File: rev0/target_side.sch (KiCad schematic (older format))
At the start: 8 parts

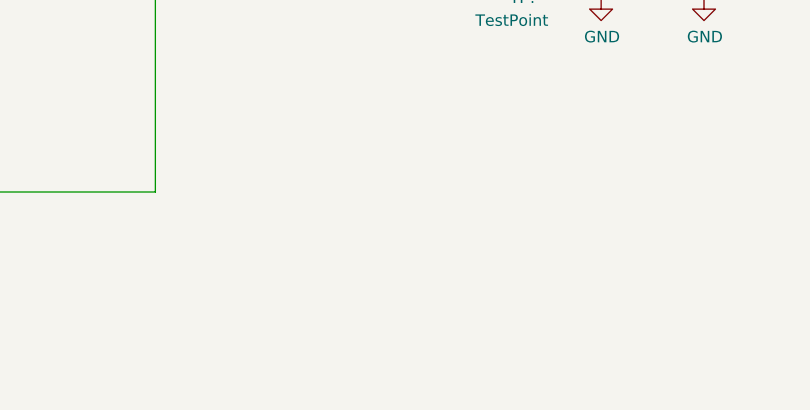
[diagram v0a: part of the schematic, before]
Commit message: schematic: finish initial capture
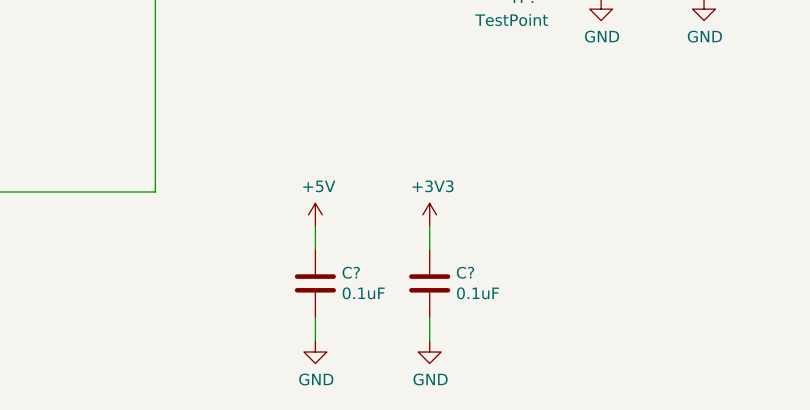
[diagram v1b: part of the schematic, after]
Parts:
- added C? (x2): 0.1uF, symbol Device:C
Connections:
- wire segments 63 -> 67
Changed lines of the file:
@@
 $Descr A4 11693 8268
 encoding utf-8
-Sheet 6 6
-Title ""
-Date ""
-Rev ""
-Comp ""
-Comment1 ""
+Sheet 5 9
+Title "LUNA: Downstream / Target / Analysis Section"
+Date "2019-10-20"
+Rev "r0"
+Comp "Great Scott Gadgets"
+Comment1 "Katherine J. Temkin"
 Comment2 ""
-Comment3 ""
+Comment3 "Licensed under the CERN OHL v1.2"
 Comment4 ""
 $EndDescr
@@
 U 1 1 5DDE2AE4
 P 6500 3750
+AR Path="/5DD754D4/5DDE2AE4" Ref="#PWR?"  Part="1"
+AR Path="/5DDDB747/5DDE2AE4" Ref="#PWR?"  Part="1"
 F 0 "#PWR?" H 6500 3600 50  0001 C CNN
 F 1 "+3V3" V 6515 3878 50  0000 L CNN
@@
 AR Path="/5DCD9772/5DDE2AF8" Ref="R?"  Part="1"
 AR Path="/5DD754D4/5DDE2AF8" Ref="R?"  Part="1"
+AR Path="/5DDDB747/5DDE2AF8" Ref="R?"  Part="1"
 F 0 "R?" V 8250 2800 50  0000 C CNN
 F 1 "20k" V 8300 2950 50  0000 C CNN
@@
 AR Path="/5DCD9772/5DDE2AFF" Ref="#PWR?"  Part="1"
 AR Path="/5DD754D4/5DDE2AFF" Ref="#PWR?"  Part="1"
+AR Path="/5DDDB747/5DDE2AFF" Ref="#PWR?"  Part="1"
 F 0 "#PWR?" H 8600 3250 50  0001 C CNN
 F 1 "GND" V 8605 3372 50  0000 R CNN
@@
 AR Path="/5DCD9772/5DDE2B06" Ref="R?"  Part="1"
 AR Path="/5DD754D4/5DDE2B06" Ref="R?"  Part="1"
+AR Path="/5DDDB747/5DDE2B06" Ref="R?"  Part="1"
 F 0 "R?" V 8200 3350 50  0000 C CNN
 F 1 "8.06k+1%" V 8150 3650 50  0000 C CNN
@@
 AR Path="/5DCD9772/5DDE2B0E" Ref="#PWR?"  Part="1"
 AR Path="/5DD754D4/5DDE2B0E" Ref="#PWR?"  Part="1"
+AR Path="/5DDDB747/5DDE2B0E" Ref="#PWR?"  Part="1"
 F 0 "#PWR?" H 8350 2150 50  0001 C CNN
 F 1 "+3V3" H 8364 2473 50  0000 C CNN
@@
 AR Path="/5DCD9772/5DDE2B14" Ref="#PWR?"  Part="1"
 AR Path="/5DD754D4/5DDE2B14" Ref="#PWR?"  Part="1"
+AR Path="/5DDDB747/5DDE2B14" Ref="#PWR?"  Part="1"
 F 0 "#PWR?" H 8150 2150 50  0001 C CNN
 F 1 "+5V" H 8164 2473 50  0000 C CNN
@@
 AR Path="/5DCD9772/5DDE2B1C" Ref="#PWR?"  Part="1"
 AR Path="/5DD754D4/5DDE2B1C" Ref="#PWR?"  Part="1"
+AR Path="/5DDDB747/5DDE2B1C" Ref="#PWR?"  Part="1"
 F 0 "#PWR?" H 8100 2500 50  0001 C CNN
 F 1 "GND" V 8105 2622 50  0000 R CNN
@@
 AR Path="/5DCD9772/5DDE2B2D" Ref="TP?"  Part="1"
 AR Path="/5DD754D4/5DDE2B2D" Ref="TP?"  Part="1"
+AR Path="/5DDDB747/5DDE2B2D" Ref="TP?"  Part="1"
 F 0 "TP?" H 8050 4600 50  0000 R CNN
 F 1 "TestPoint" H 8200 4700 50  0000 R CNN
@@
 AR Path="/5DCD9772/5DDE2B37" Ref="TP?"  Part="1"
 AR Path="/5DD754D4/5DDE2B37" Ref="TP?"  Part="1"
+AR Path="/5DDDB747/5DDE2B37" Ref="TP?"  Part="1"
 F 0 "TP?" V 9055 4087 50  0000 L CNN
 F 1 "TestPoint" V 9145 4087 50  0000 L CNN
@@
 AR Path="/5DCD9772/5DDE2B42" Ref="#PWR?"  Part="1"
 AR Path="/5DD754D4/5DDE2B42" Ref="#PWR?"  Part="1"
+AR Path="/5DDDB747/5DDE2B42" Ref="#PWR?"  Part="1"
 F 0 "#PWR?" H 8800 4350 50  0001 C CNN
 F 1 "GND" H 8804 4428 50  0000 C CNN
@@
 AR Path="/5DCD9772/5DDE2B48" Ref="C?"  Part="1"
 AR Path="/5DD754D4/5DDE2B48" Ref="C?"  Part="1"
+AR Path="/5DDDB747/5DDE2B48" Ref="C?"  Part="1"
 F 0 "C?" H 8915 4345 50  0000 L CNN
 F 1 "1uF" H 8915 4255 50  0000 L CNN
@@
 AR Path="/5DCD9772/5DDE2B50" Ref="#PWR?"  Part="1"
 AR Path="/5DD754D4/5DDE2B50" Ref="#PWR?"  Part="1"
+AR Path="/5DDDB747/5DDE2B50" Ref="#PWR?"  Part="1"
 F 0 "#PWR?" H 8350 4350 50  0001 C CNN
 F 1 "GND" H 8354 4428 50  0000 C CNN
@@
 AR Path="/5DCD9772/5DDE2B56" Ref="C?"  Part="1"
 AR Path="/5DD754D4/5DDE2B56" Ref="C?"  Part="1"
+AR Path="/5DDDB747/5DDE2B56" Ref="C?"  Part="1"
 F 0 "C?" H 8465 4345 50  0000 L CNN
 F 1 "1uF" H 8465 4255 50  0000 L CNN
@@
 AR Path="/5DCD9772/5DDE2B63" Ref="U?"  Part="1"
 AR Path="/5DD754D4/5DDE2B63" Ref="U?"  Part="1"
+AR Path="/5DDDB747/5DDE2B63" Ref="U?"  Part="1"
 F 0 "U?" H 7250 2613 50  0000 C CNN
 F 1 "USB3343" H 7250 2523 50  0000 C CNN
@@
 	1    0    0    -1
 $EndComp
+$Comp
+L Device:C C?
+U 1 1 5DEDF6B3
+P 7100 5850
+AR Path="/5DCD9772/5DEDF6B3" Ref="C?"  Part="1"
+AR Path="/5DDDB747/5DEDF6B3" Ref="C?"  Part="1"
+F 0 "C?" H 7215 5895 50  0000 L CNN
+F 1 "0.1uF" H 7215 5805 50  0000 L CNN
+F 2 "" H 7138 5700 50  0001 C CNN
+F 3 "~" H 7100 5850 50  0001 C CNN
+	1    7100 5850
+	1    0    0    -1
+$EndComp
+$Comp
+L Device:C C?
+U 1 1 5DEDF6B9
+P 7600 5850
+AR Path="/5DCD9772/5DEDF6B9" Ref="C?"  Part="1"
+AR Path="/5DDDB747/5DEDF6B9" Ref="C?"  Part="1"
+F 0 "C?" H 7715 5895 50  0000 L CNN
+F 1 "0.1uF" H 7715 5805 50  0000 L CNN
+F 2 "" H 7638 5700 50  0001 C CNN
+F 3 "~" H 7600 5850 50  0001 C CNN
+	1    7600 5850
+	1    0    0    -1
+$EndComp
+$Comp
+L power:+5V #PWR?
+U 1 1 5DEDF6BF
+P 7100 5600
+AR Path="/5DCD9772/5DEDF6BF" Ref="#PWR?"  Part="1"
+AR Path="/5DDDB747/5DEDF6BF" Ref="#PWR?"  Part="1"
+F 0 "#PWR?" H 7100 5450 50  0001 C CNN
+F 1 "+5V" H 7114 5773 50  0000 C CNN
+F 2 "" H 7100 5600 50  0001 C CNN
+F 3 "" H 7100 5600 50  0001 C CNN
+	1    7100 5600
+	1    0    0    -1
+$EndComp
+$Comp
+L power:+3V3 #PWR?
+U 1 1 5DEDF6C5
+P 7600 5600
+AR Path="/5DCD9772/5DEDF6C5" Ref="#PWR?"  Part="1"
+AR Path="/5DDDB747/5DEDF6C5" Ref="#PWR?"  Part="1"
+F 0 "#PWR?" H 7600 5450 50  0001 C CNN
+F 1 "+3V3" H 7614 5773 50  0000 C CNN
+F 2 "" H 7600 5600 50  0001 C CNN
+F 3 "" H 7600 5600 50  0001 C CNN
+	1    7600 5600
+	1    0    0    -1
+$EndComp
+$Comp
+L power:GND #PWR?
+U 1 1 5DEDF6CB
+P 7100 6100
+AR Path="/5DCD9772/5DEDF6CB" Ref="#PWR?"  Part="1"
+AR Path="/5DDDB747/5DEDF6CB" Ref="#PWR?"  Part="1"
+F 0 "#PWR?" H 7100 5850 50  0001 C CNN
+F 1 "GND" H 7104 5928 50  0000 C CNN
+F 2 "" H 7100 6100 50  0001 C CNN
+F 3 "" H 7100 6100 50  0001 C CNN
+	1    7100 6100
+	1    0    0    -1
+$EndComp
+$Comp
+L power:GND #PWR?
+U 1 1 5DEDF6D1
+P 7600 6100
+AR Path="/5DCD9772/5DEDF6D1" Ref="#PWR?"  Part="1"
+AR Path="/5DDDB747/5DEDF6D1" Ref="#PWR?"  Part="1"
+F 0 "#PWR?" H 7600 5850 50  0001 C CNN
+F 1 "GND" H 7604 5928 50  0000 C CNN
+F 2 "" H 7600 6100 50  0001 C CNN
+F 3 "" H 7600 6100 50  0001 C CNN
+	1    7600 6100
+	1    0    0    -1
+$EndComp
+Wire Wire Line
+	7600 5600 7600 5700
+Wire Wire Line
+	7100 5600 7100 5700
+Wire Wire Line
+	7100 6000 7100 6100
+Wire Wire Line
+	7600 6000 7600 6100
 $EndSCHEMATC

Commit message: rev0: finish capture and start routing (woo!)
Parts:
- added R23: 10K, Resistor_SMD:R_0402_1005Metric, symbol Device:R
- C40, C41: renamed from C?; footprint (none) -> Capacitor_SMD:C_0402_1005Metric
- C42, C43: renamed from C?; footprint (none) -> Capacitor_SMD:C_0603_1608Metric
- IC1: renamed from IC?; footprint BGA256C80P16X16_1400X1400X170 -> luna:lattice_cabga256
- R18, R19: renamed from R?; footprint (none) -> Resistor_SMD:R_0402_1005Metric
- TP7, TP8: renamed from TP?; footprint (none) -> TestPoint:TestPoint_Pad_1.0x1.0mm
- U9: renamed from U?; footprint (none) -> Package_DFN_QFN:VQFN-24-1EP_4x4mm_P0.5mm_EP2.45x2.45mm
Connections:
- net labels added: +3.3V
- wire segments 67 -> 70
- no-connect marks 19 -> 20
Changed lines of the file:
@@
 P 6500 3750
 AR Path="/5DD754D4/5DDE2AE4" Ref="#PWR?"  Part="1"
-AR Path="/5DDDB747/5DDE2AE4" Ref="#PWR?"  Part="1"
-F 0 "#PWR?" H 6500 3600 50  0001 C CNN
+AR Path="/5DDDB747/5DDE2AE4" Ref="#PWR070"  Part="1"
+F 0 "#PWR070" H 6500 3600 50  0001 C CNN
 F 1 "+3V3" V 6515 3878 50  0000 L CNN
 F 2 "" H 6500 3750 50  0001 C CNN
@@
 AR Path="/5DCD9772/5DDE2AF8" Ref="R?"  Part="1"
 AR Path="/5DD754D4/5DDE2AF8" Ref="R?"  Part="1"
-AR Path="/5DDDB747/5DDE2AF8" Ref="R?"  Part="1"
-F 0 "R?" V 8250 2800 50  0000 C CNN
+AR Path="/5DDDB747/5DDE2AF8" Ref="R19"  Part="1"
+F 0 "R19" V 8250 2800 50  0000 C CNN
 F 1 "20k" V 8300 2950 50  0000 C CNN
-F 2 "" V 8230 2950 50  0001 C CNN
+F 2 "Resistor_SMD:R_0402_1005Metric" V 8230 2950 50  0001 C CNN
 F 3 "~" H 8300 2950 50  0001 C CNN
 	1    8300 2950
@@
 AR Path="/5DCD9772/5DDE2AFF" Ref="#PWR?"  Part="1"
 AR Path="/5DD754D4/5DDE2AFF" Ref="#PWR?"  Part="1"
-AR Path="/5DDDB747/5DDE2AFF" Ref="#PWR?"  Part="1"
-F 0 "#PWR?" H 8600 3250 50  0001 C CNN
+AR Path="/5DDDB747/5DDE2AFF" Ref="#PWR079"  Part="1"
+F 0 "#PWR079" H 8600 3250 50  0001 C CNN
 F 1 "GND" V 8605 3372 50  0000 R CNN
 F 2 "" H 8600 3500 50  0001 C CNN
@@
 AR Path="/5DCD9772/5DDE2B06" Ref="R?"  Part="1"
 AR Path="/5DD754D4/5DDE2B06" Ref="R?"  Part="1"
-AR Path="/5DDDB747/5DDE2B06" Ref="R?"  Part="1"
-F 0 "R?" V 8200 3350 50  0000 C CNN
+AR Path="/5DDDB747/5DDE2B06" Ref="R18"  Part="1"
+F 0 "R18" V 8200 3350 50  0000 C CNN
 F 1 "8.06k+1%" V 8150 3650 50  0000 C CNN
-F 2 "" V 8180 3500 50  0001 C CNN
+F 2 "Resistor_SMD:R_0402_1005Metric" V 8180 3500 50  0001 C CNN
 F 3 "~" H 8250 3500 50  0001 C CNN
 	1    8250 3500
@@
 AR Path="/5DCD9772/5DDE2B0E" Ref="#PWR?"  Part="1"
 AR Path="/5DD754D4/5DDE2B0E" Ref="#PWR?"  Part="1"
-AR Path="/5DDDB747/5DDE2B0E" Ref="#PWR?"  Part="1"
-F 0 "#PWR?" H 8350 2150 50  0001 C CNN
+AR Path="/5DDDB747/5DDE2B0E" Ref="#PWR077"  Part="1"
+F 0 "#PWR077" H 8350 2150 50  0001 C CNN
 F 1 "+3V3" H 8364 2473 50  0000 C CNN
 F 2 "" H 8350 2300 50  0001 C CNN
@@
 AR Path="/5DCD9772/5DDE2B14" Ref="#PWR?"  Part="1"
 AR Path="/5DD754D4/5DDE2B14" Ref="#PWR?"  Part="1"
-AR Path="/5DDDB747/5DDE2B14" Ref="#PWR?"  Part="1"
-F 0 "#PWR?" H 8150 2150 50  0001 C CNN
+AR Path="/5DDDB747/5DDE2B14" Ref="#PWR076"  Part="1"
+F 0 "#PWR076" H 8150 2150 50  0001 C CNN
 F 1 "+5V" H 8164 2473 50  0000 C CNN
 F 2 "" H 8150 2300 50  0001 C CNN
@@
 AR Path="/5DCD9772/5DDE2B1C" Ref="#PWR?"  Part="1"
 AR Path="/5DD754D4/5DDE2B1C" Ref="#PWR?"  Part="1"
-AR Path="/5DDDB747/5DDE2B1C" Ref="#PWR?"  Part="1"
-F 0 "#PWR?" H 8100 2500 50  0001 C CNN
+AR Path="/5DDDB747/5DDE2B1C" Ref="#PWR075"  Part="1"
+F 0 "#PWR075" H 8100 2500 50  0001 C CNN
 F 1 "GND" V 8105 2622 50  0000 R CNN
 F 2 "" H 8100 2750 50  0001 C CNN
@@
 AR Path="/5DCD9772/5DDE2B2D" Ref="TP?"  Part="1"
 AR Path="/5DD754D4/5DDE2B2D" Ref="TP?"  Part="1"
-AR Path="/5DDDB747/5DDE2B2D" Ref="TP?"  Part="1"
-F 0 "TP?" H 8050 4600 50  0000 R CNN
+AR Path="/5DDDB747/5DDE2B2D" Ref="TP7"  Part="1"
+F 0 "TP7" H 8050 4600 50  0000 R CNN
 F 1 "TestPoint" H 8200 4700 50  0000 R CNN
-F 2 "" H 8200 4350 50  0001 C CNN
+F 2 "TestPoint:TestPoint_Pad_1.0x1.0mm" H 8200 4350 50  0001 C CNN
 F 3 "~" H 8200 4350 50  0001 C CNN
 	1    8000 4350
@@
 AR Path="/5DCD9772/5DDE2B37" Ref="TP?"  Part="1"
 AR Path="/5DD754D4/5DDE2B37" Ref="TP?"  Part="1"
-AR Path="/5DDDB747/5DDE2B37" Ref="TP?"  Part="1"
-F 0 "TP?" V 9055 4087 50  0000 L CNN
+AR Path="/5DDDB747/5DDE2B37" Ref="TP8"  Part="1"
+F 0 "TP8" V 9055 4087 50  0000 L CNN
 F 1 "TestPoint" V 9145 4087 50  0000 L CNN
-F 2 "" H 9300 3900 50  0001 C CNN
+F 2 "TestPoint:TestPoint_Pad_1.0x1.0mm" H 9300 3900 50  0001 C CNN
 F 3 "~" H 9300 3900 50  0001 C CNN
 	1    9100 3900
@@
 AR Path="/5DCD9772/5DDE2B42" Ref="#PWR?"  Part="1"
 AR Path="/5DD754D4/5DDE2B42" Ref="#PWR?"  Part="1"
-AR Path="/5DDDB747/5DDE2B42" Ref="#PWR?"  Part="1"
-F 0 "#PWR?" H 8800 4350 50  0001 C CNN
+AR Path="/5DDDB747/5DDE2B42" Ref="#PWR080"  Part="1"
+F 0 "#PWR080" H 8800 4350 50  0001 C CNN
 F 1 "GND" H 8804 4428 50  0000 C CNN
 F 2 "" H 8800 4600 50  0001 C CNN
@@
 AR Path="/5DCD9772/5DDE2B48" Ref="C?"  Part="1"
 AR Path="/5DD754D4/5DDE2B48" Ref="C?"  Part="1"
-AR Path="/5DDDB747/5DDE2B48" Ref="C?"  Part="1"
-F 0 "C?" H 8915 4345 50  0000 L CNN
+AR Path="/5DDDB747/5DDE2B48" Ref="C43"  Part="1"
+F 0 "C43" H 8915 4345 50  0000 L CNN
 F 1 "1uF" H 8915 4255 50  0000 L CNN
-F 2 "" H 8838 4150 50  0001 C CNN
+F 2 "Capacitor_SMD:C_0603_1608Metric" H 8838 4150 50  0001 C CNN
 F 3 "~" H 8800 4300 50  0001 C CNN
 	1    8800 4300
@@
 AR Path="/5DCD9772/5DDE2B50" Ref="#PWR?"  Part="1"
 AR Path="/5DD754D4/5DDE2B50" Ref="#PWR?"  Part="1"
-AR Path="/5DDDB747/5DDE2B50" Ref="#PWR?"  Part="1"
-F 0 "#PWR?" H 8350 4350 50  0001 C CNN
+AR Path="/5DDDB747/5DDE2B50" Ref="#PWR078"  Part="1"
+F 0 "#PWR078" H 8350 4350 50  0001 C CNN
 F 1 "GND" H 8354 4428 50  0000 C CNN
 F 2 "" H 8350 4600 50  0001 C CNN
@@
 AR Path="/5DCD9772/5DDE2B56" Ref="C?"  Part="1"
 AR Path="/5DD754D4/5DDE2B56" Ref="C?"  Part="1"
-AR Path="/5DDDB747/5DDE2B56" Ref="C?"  Part="1"
-F 0 "C?" H 8465 4345 50  0000 L CNN
+AR Path="/5DDDB747/5DDE2B56" Ref="C42"  Part="1"
+F 0 "C42" H 8465 4345 50  0000 L CNN
 F 1 "1uF" H 8465 4255 50  0000 L CNN
-F 2 "" H 8388 4150 50  0001 C CNN
+F 2 "Capacitor_SMD:C_0603_1608Metric" H 8388 4150 50  0001 C CNN
 F 3 "~" H 8350 4300 50  0001 C CNN
 	1    8350 4300
@@
 AR Path="/5DCD9772/5DDE2B63" Ref="U?"  Part="1"
 AR Path="/5DD754D4/5DDE2B63" Ref="U?"  Part="1"
-AR Path="/5DDDB747/5DDE2B63" Ref="U?"  Part="1"
-F 0 "U?" H 7250 2613 50  0000 C CNN
+AR Path="/5DDDB747/5DDE2B63" Ref="U9"  Part="1"
+F 0 "U9" H 7250 2613 50  0000 C CNN
 F 1 "USB3343" H 7250 2523 50  0000 C CNN
-F 2 "" H 6650 2450 50  0001 C CNN
+F 2 "Package_DFN_QFN:VQFN-24-1EP_4x4mm_P0.5mm_EP2.45x2.45mm" H 6650 2450 50  0001 C CNN
 F 3 "http://ww1.microchip.com/downloads/en/DeviceDoc/334x.pdf" H 6650 2450 50  0001 C CNN
 	1    6650 2450
@@
 $EndComp
 $Comp
-L fpgas_and_processors:ECP5-BGA256 IC?
+L fpgas_and_processors:ECP5-BGA256 IC1
 U 4 1 5DDE3D5A
 P 1650 2100
-F 0 "IC?" H 1620 283 50  0000 R CNN
+F 0 "IC1" H 1620 283 50  0000 R CNN
 F 1 "ECP5-BGA256" H 1620 193 50  0000 R CNN
-F 2 "BGA256C80P16X16_1400X1400X170" H -1550 5550 50  0001 L CNN
+F 2 "luna:lattice_cabga256" H -1550 5550 50  0001 L CNN
 F 3 "" H -2000 6500 50  0001 L CNN
 F 4 "FPGA - Field Programmable Gate Array ECP5; 12k LUTs; 1.1V" H -2000 6400 50  0001 L CNN "Description"
@@
 Wire Wire Line
 	5500 5350 2600 5350
-Wire Wire Line
-	6400 5450 2600 5450
 Wire Wire Line
 	6400 4000 6400 5450
@@
 	1850 1800 1900 1800
 $Comp
-L power:+3V3 #PWR?
+L power:+3V3 #PWR069
 U 1 1 5DE347EF
 P 1850 1700
-F 0 "#PWR?" H 1850 1550 50  0001 C CNN
+F 0 "#PWR069" H 1850 1550 50  0001 C CNN
 F 1 "+3V3" H 1864 1873 50  0000 C CNN
 F 2 "" H 1850 1700 50  0001 C CNN
@@
 P 7100 5850
 AR Path="/5DCD9772/5DEDF6B3" Ref="C?"  Part="1"
-AR Path="/5DDDB747/5DEDF6B3" Ref="C?"  Part="1"
-F 0 "C?" H 7215 5895 50  0000 L CNN
+AR Path="/5DDDB747/5DEDF6B3" Ref="C40"  Part="1"
+F 0 "C40" H 7215 5895 50  0000 L CNN
 F 1 "0.1uF" H 7215 5805 50  0000 L CNN
-F 2 "" H 7138 5700 50  0001 C CNN
+F 2 "Capacitor_SMD:C_0402_1005Metric" H 7138 5700 50  0001 C CNN
 F 3 "~" H 7100 5850 50  0001 C CNN
 	1    7100 5850
@@
 P 7600 5850
 AR Path="/5DCD9772/5DEDF6B9" Ref="C?"  Part="1"
-AR Path="/5DDDB747/5DEDF6B9" Ref="C?"  Part="1"
-F 0 "C?" H 7715 5895 50  0000 L CNN
+AR Path="/5DDDB747/5DEDF6B9" Ref="C41"  Part="1"
+F 0 "C41" H 7715 5895 50  0000 L CNN
 F 1 "0.1uF" H 7715 5805 50  0000 L CNN
-F 2 "" H 7638 5700 50  0001 C CNN
+F 2 "Capacitor_SMD:C_0402_1005Metric" H 7638 5700 50  0001 C CNN
 F 3 "~" H 7600 5850 50  0001 C CNN
 	1    7600 5850
@@
 P 7100 5600
 AR Path="/5DCD9772/5DEDF6BF" Ref="#PWR?"  Part="1"
-AR Path="/5DDDB747/5DEDF6BF" Ref="#PWR?"  Part="1"
-F 0 "#PWR?" H 7100 5450 50  0001 C CNN
+AR Path="/5DDDB747/5DEDF6BF" Ref="#PWR071"  Part="1"
+F 0 "#PWR071" H 7100 5450 50  0001 C CNN
 F 1 "+5V" H 7114 5773 50  0000 C CNN
 F 2 "" H 7100 5600 50  0001 C CNN
@@
 P 7600 5600
 AR Path="/5DCD9772/5DEDF6C5" Ref="#PWR?"  Part="1"
-AR Path="/5DDDB747/5DEDF6C5" Ref="#PWR?"  Part="1"
-F 0 "#PWR?" H 7600 5450 50  0001 C CNN
+AR Path="/5DDDB747/5DEDF6C5" Ref="#PWR073"  Part="1"
+F 0 "#PWR073" H 7600 5450 50  0001 C CNN
 F 1 "+3V3" H 7614 5773 50  0000 C CNN
 F 2 "" H 7600 5600 50  0001 C CNN
@@
 P 7100 6100
 AR Path="/5DCD9772/5DEDF6CB" Ref="#PWR?"  Part="1"
-AR Path="/5DDDB747/5DEDF6CB" Ref="#PWR?"  Part="1"
-F 0 "#PWR?" H 7100 5850 50  0001 C CNN
+AR Path="/5DDDB747/5DEDF6CB" Ref="#PWR072"  Part="1"
+F 0 "#PWR072" H 7100 5850 50  0001 C CNN
 F 1 "GND" H 7104 5928 50  0000 C CNN
 F 2 "" H 7100 6100 50  0001 C CNN
@@
 P 7600 6100
 AR Path="/5DCD9772/5DEDF6D1" Ref="#PWR?"  Part="1"
-AR Path="/5DDDB747/5DEDF6D1" Ref="#PWR?"  Part="1"
-F 0 "#PWR?" H 7600 5850 50  0001 C CNN
+AR Path="/5DDDB747/5DEDF6D1" Ref="#PWR074"  Part="1"
+F 0 "#PWR074" H 7600 5850 50  0001 C CNN
 F 1 "GND" H 7604 5928 50  0000 C CNN
 F 2 "" H 7600 6100 50  0001 C CNN
@@
 Wire Wire Line
 	7600 6000 7600 6100
+$Comp
+L Device:R R?
+U 1 1 5E15EF0F
+P 5900 5200
+AR Path="/5DD754D4/5E15EF0F" Ref="R?"  Part="1"
+AR Path="/5DDDB747/5E15EF0F" Ref="R23"  Part="1"
+F 0 "R23" V 6000 5200 50  0000 C CNN
+F 1 "10K" V 5900 5200 50  0000 C CNN
+F 2 "Resistor_SMD:R_0402_1005Metric" V 5830 5200 50  0001 C CNN
+F 3 "~" H 5900 5200 50  0001 C CNN
+	1    5900 5200
+	-1   0    0    1
+$EndComp
+Wire Wire Line
+	5900 5350 5900 5450
+Wire Wire Line
+	5900 5050 5900 4950
+$Comp
+L ibp-hyperram-cache:+3.3V #PWR?
+U 1 1 5E15EF17
+P 5900 4950
+AR Path="/5DD754D4/5E15EF17" Ref="#PWR?"  Part="1"
+AR Path="/5DDDB747/5E15EF17" Ref="#PWR0100"  Part="1"
+F 0 "#PWR0100" H 5900 4800 50  0001 C CNN
+F 1 "+3.3V" V 5915 5078 50  0000 L CNN
+F 2 "" H 5900 4950 50  0001 C CNN
+F 3 "" H 5900 4950 50  0001 C CNN
+	1    5900 4950
+	1    0    0    -1
+$EndComp
+Wire Wire Line
+	2600 5450 5900 5450
+Connection ~ 5900 5450
+Wire Wire Line
+	5900 5450 6400 5450
+NoConn ~ 7950 3700
 $EndSCHEMATC

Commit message: rev0: clean up library references and backup files
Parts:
- U9: symbol rhododendron:USB3343 -> usb:USB3343
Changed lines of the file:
@@
 EESchema Schematic File Version 4
 LIBS:luna_rev0-cache
-EELAYER 29 0
+EELAYER 30 0
 EELAYER END
 $Descr A4 11693 8268
@@
 	7950 3800 8850 3800
 $Comp
-L rhododendron:USB3343 U?
+L usb:USB3343 U?
 U 1 1 5DDE2B63
 P 6650 2450
@@
 	5900 5050 5900 4950
 $Comp
-L ibp-hyperram-cache:+3.3V #PWR?
+L support_hardware:S27KS0641 #PWR?
 U 1 1 5E15EF17
 P 5900 4950
 AR Path="/5DD754D4/5E15EF17" Ref="#PWR?"  Part="1"
 AR Path="/5DDDB747/5E15EF17" Ref="#PWR0100"  Part="1"
+AR Path="/5E15EF17" Ref="#PWR0100"  Part="1"
 F 0 "#PWR0100" H 5900 4800 50  0001 C CNN
 F 1 "+3.3V" V 5915 5078 50  0000 L CNN
